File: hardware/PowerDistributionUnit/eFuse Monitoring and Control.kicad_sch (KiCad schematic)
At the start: 103 parts, among them U34 MCP23017_SO, U37 MCP23017_SO, U38 ADS131M08-Q1, U39 ADS131M08-Q1, Y1 ABM3-8.000MHZ-D2Y-T

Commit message: schematic updated
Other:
- company: (none) -> Longhorn Racing Solar
- title: (none) -> eFuse Monitoring and Control
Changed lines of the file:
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@@
 	(generator_version "9.0")
 	(paper "A4")
+	(title_block
+		(title "eFuse Monitoring and Control")
+		(date "2025-04-17")
+		(rev "A")
+		(company "Longhorn Racing Solar")
+		(comment 1 "Changxu Liu, Watts Yasueda")
+	)
 	(rectangle
 		(start 19.05 15.24)
@@
 		)
 		(instances
-			(project ""
+			(project "PowerDistributionUnit"
 				(path "/93fa4ef0-f02c-4535-aca9-c62461ff58dd/afc26468-877c-4928-9f2e-9c48c52cd2d4/bc39789f-e0c1-41b2-a007-8436ff69f871"
 					(reference "U34")

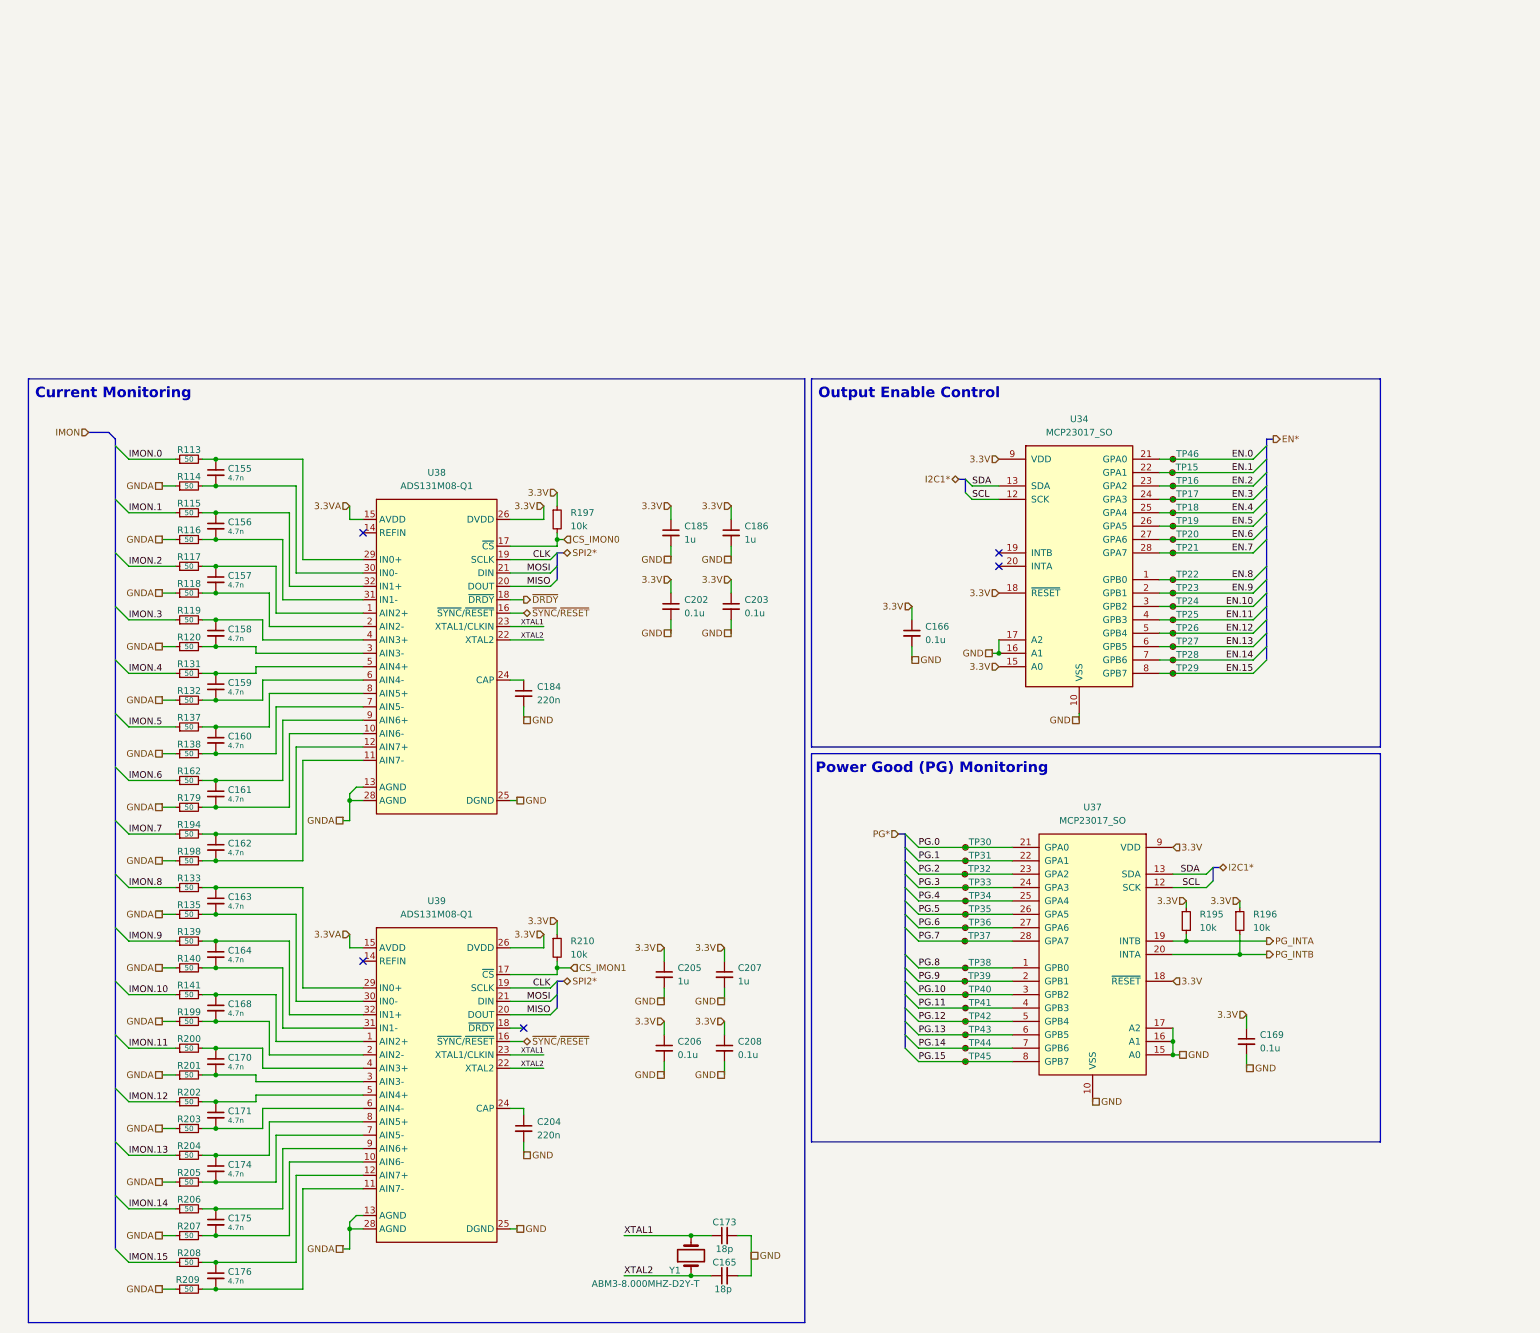
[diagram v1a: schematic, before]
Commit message: started layout for general and eFuses, corrected schematic (test point footprints, bus label names, connection points, etc.), corrected footprint courtyard (eFuse, diode)
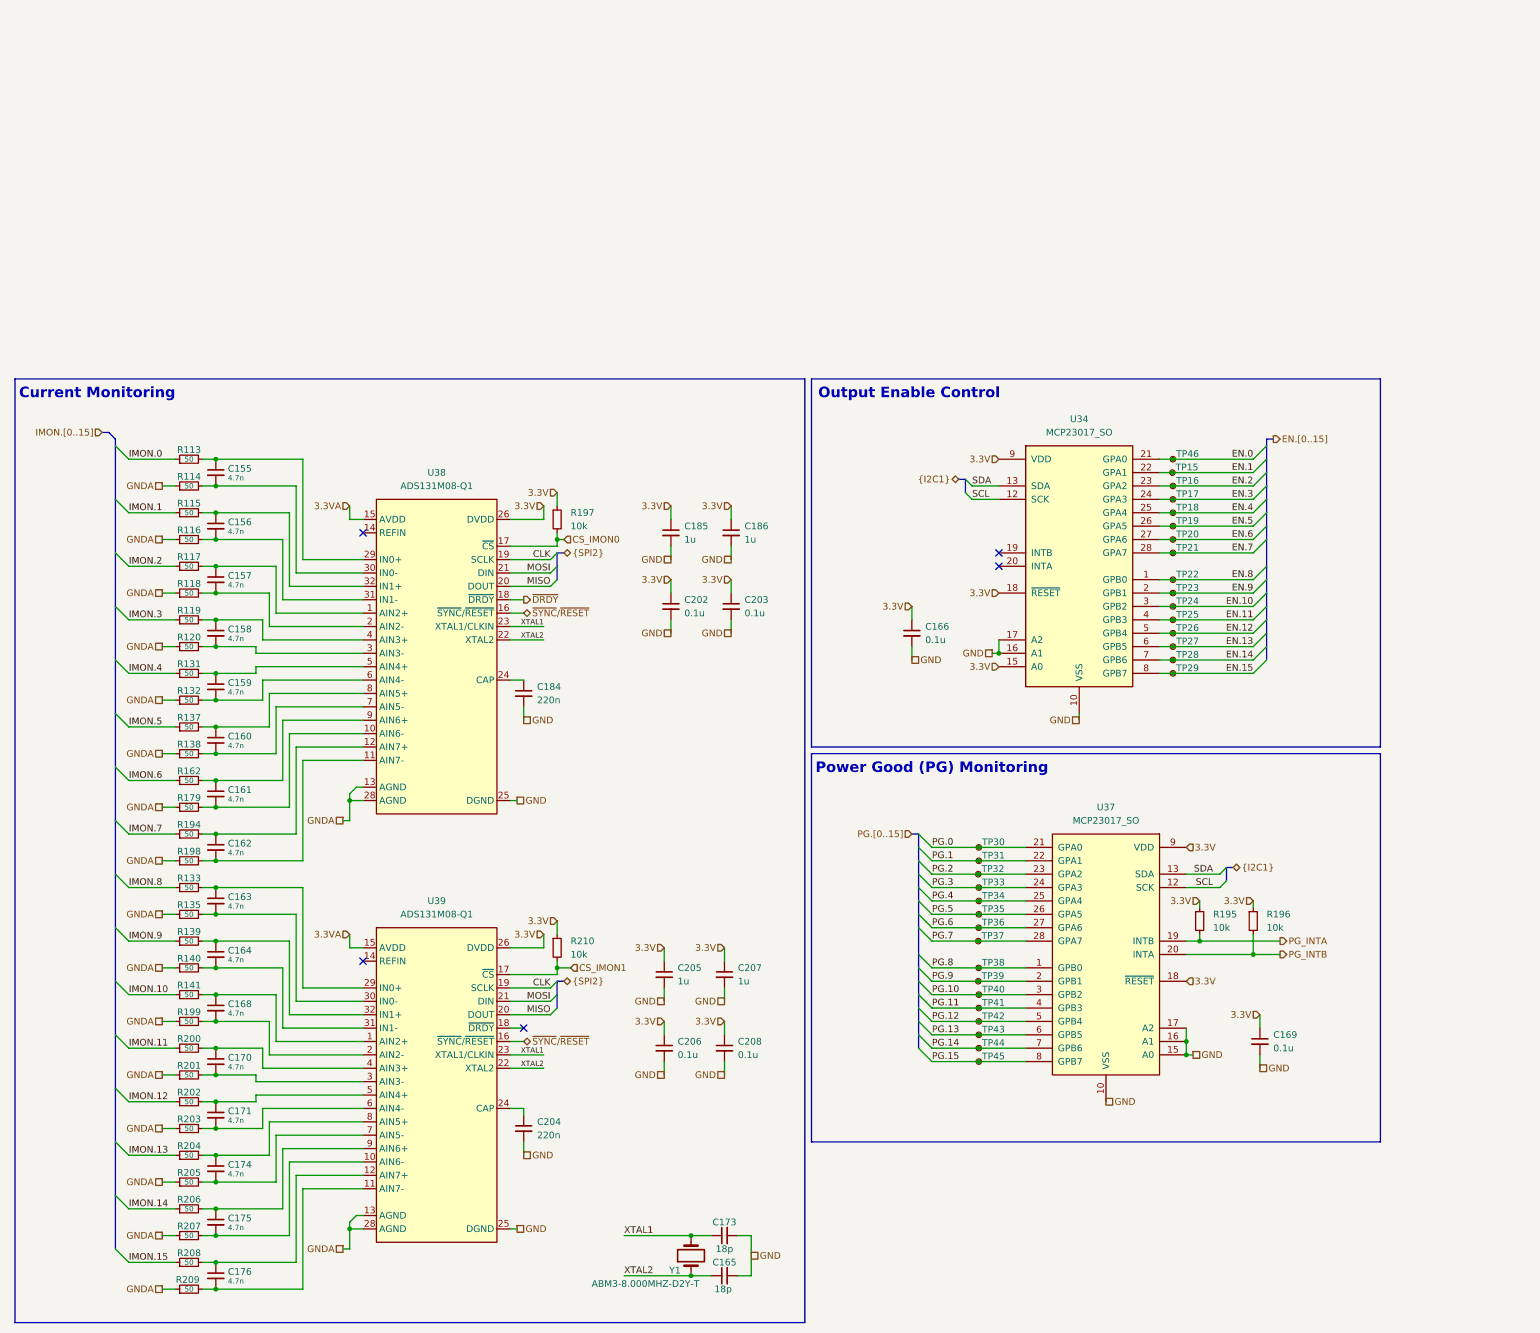
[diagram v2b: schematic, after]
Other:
- moved on the sheet: C169, R195, R196, TP30, TP31, TP32, TP33, TP34, TP35, TP36, TP37, TP38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

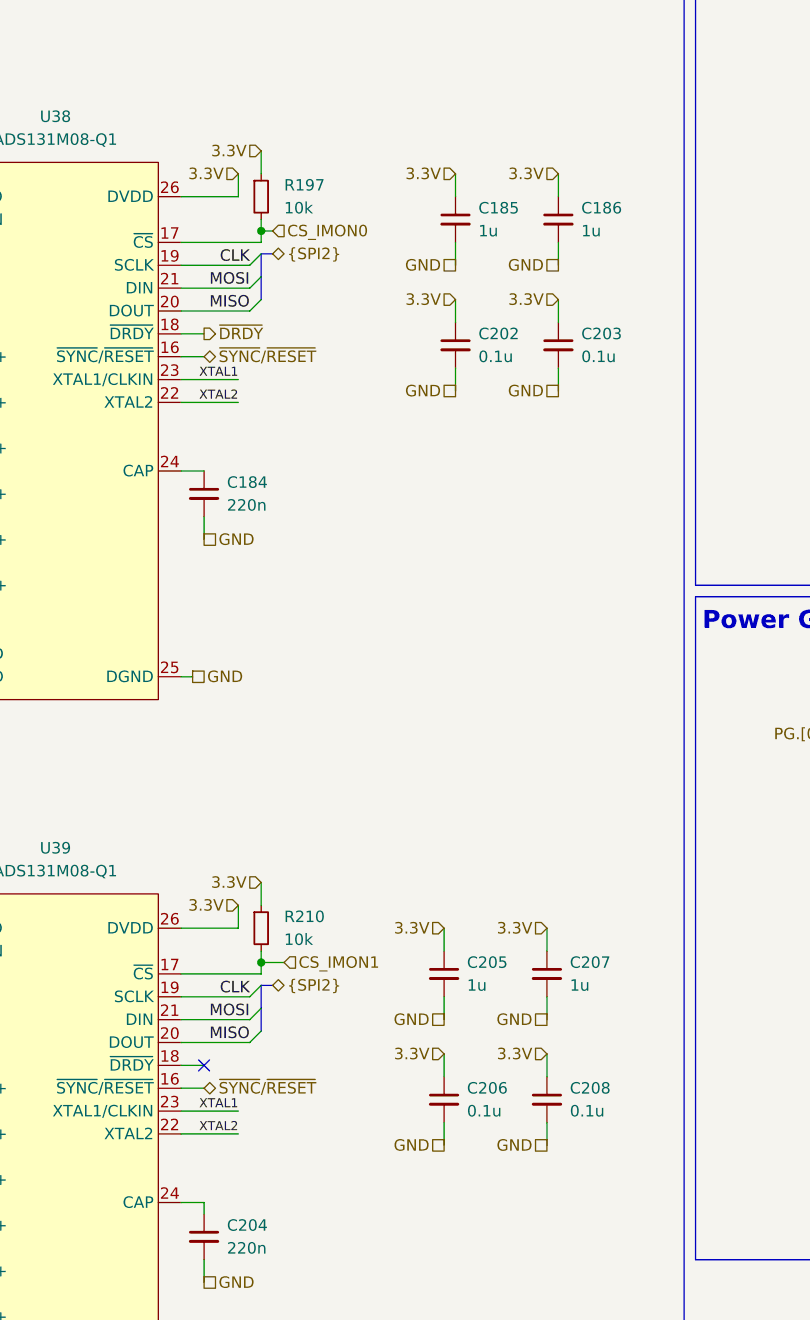
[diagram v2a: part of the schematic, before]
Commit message: Updated GND and 3.3V to GNDA and 3.3VA. Made progress on layout for current monitoring components
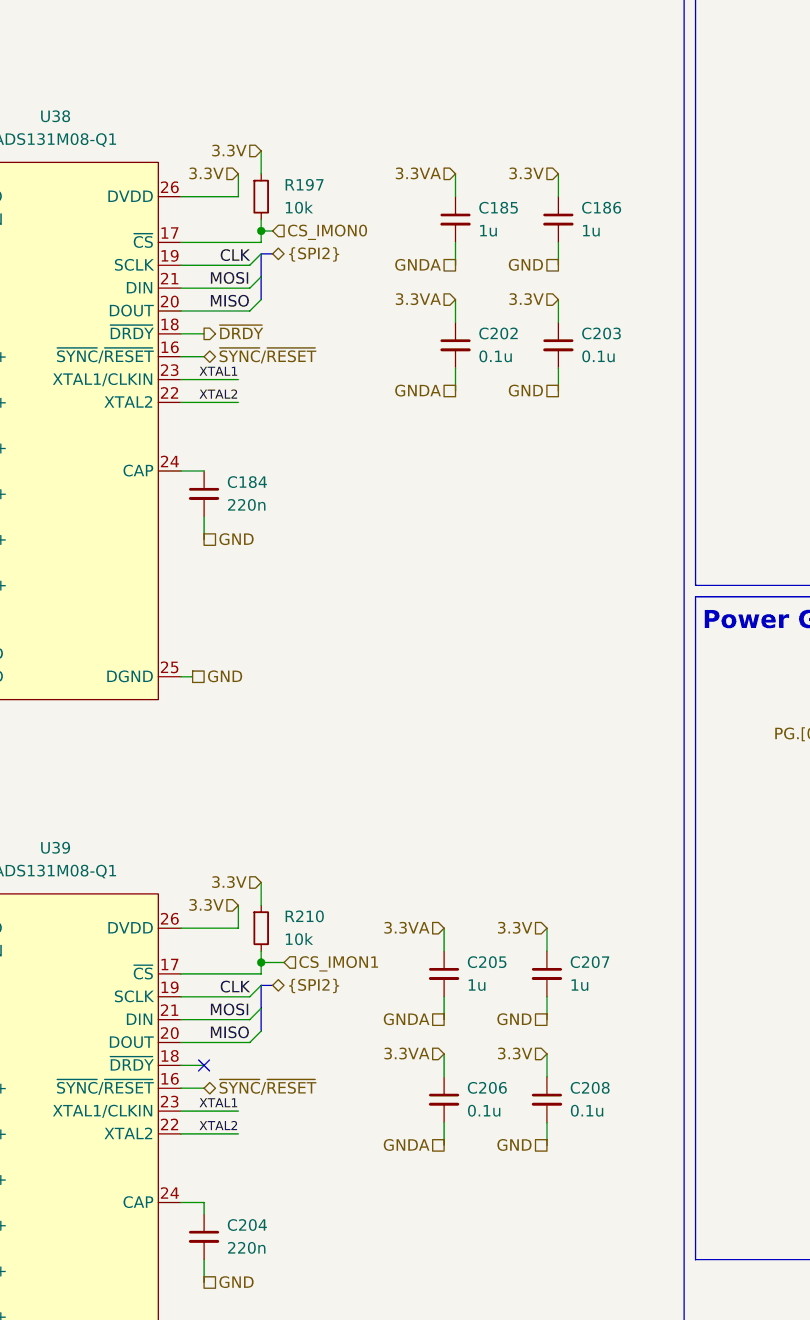
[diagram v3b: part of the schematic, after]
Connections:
- net 3.3V: no longer C185.1, C202.1, C205.1, C206.1
- net 3.3VA: now also C185.1, C202.1, C205.1, C206.1
- net GND: no longer C185.2, C202.2, C205.2, C206.2
- net GNDA: now also C185.2, C202.2, C205.2, C206.2
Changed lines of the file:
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@@
 		)
 	)
-	(hierarchical_label "3.3V"
+	(hierarchical_label "3.3VA"
 		(shape input)
 		(at 140.97 39.37 180)
@@
 		)
 	)
-	(hierarchical_label "3.3V"
+	(hierarchical_label "3.3VA"
 		(shape input)
 		(at 140.97 53.34 180)
@@
 		)
 	)
-	(hierarchical_label "GND"
+	(hierarchical_label "GNDA"
 		(shape passive)
 		(at 139.7 147.32 180)
@@
 		)
 	)
-	(hierarchical_label "GND"
+	(hierarchical_label "GNDA"
 		(shape passive)
 		(at 140.97 63.5 180)
@@
 		)
 	)
-	(hierarchical_label "3.3V"
+	(hierarchical_label "3.3VA"
 		(shape input)
 		(at 139.7 137.16 180)
@@
 		)
 	)
-	(hierarchical_label "GND"
+	(hierarchical_label "GNDA"
 		(shape passive)
 		(at 140.97 49.53 180)
@@
 		)
 	)
-	(hierarchical_label "GND"
+	(hierarchical_label "GNDA"
 		(shape passive)
 		(at 139.7 133.35 180)
@@
 		)
 	)
-	(hierarchical_label "3.3V"
+	(hierarchical_label "3.3VA"
 		(shape input)
 		(at 139.7 123.19 180)
